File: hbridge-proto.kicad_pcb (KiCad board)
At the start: 2 copper layers, 126 x 72 mm, 45 parts, among them IC1 LM5106, IC2 LM5106, J1 Screw_Terminal_1x03, J2 Screw_Terminal_1x02, J3 Screw_Terminal_1x02, J4 Screw_Terminal_1x02, Q1 TO-220-DUAL, Q2 TO-220-DUAL, Q3 TO-220-DUAL, Q4 TO-220-DUAL

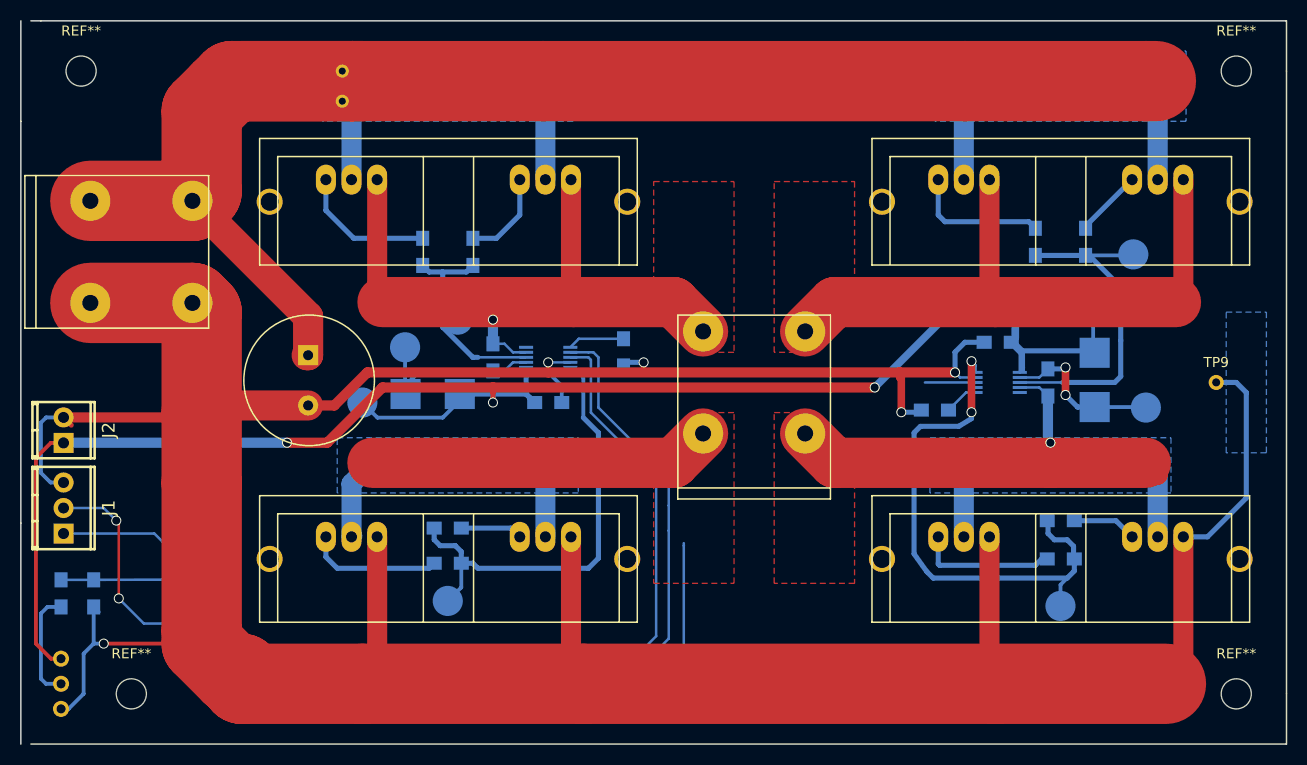
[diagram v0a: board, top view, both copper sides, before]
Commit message: Improved driver signal routing
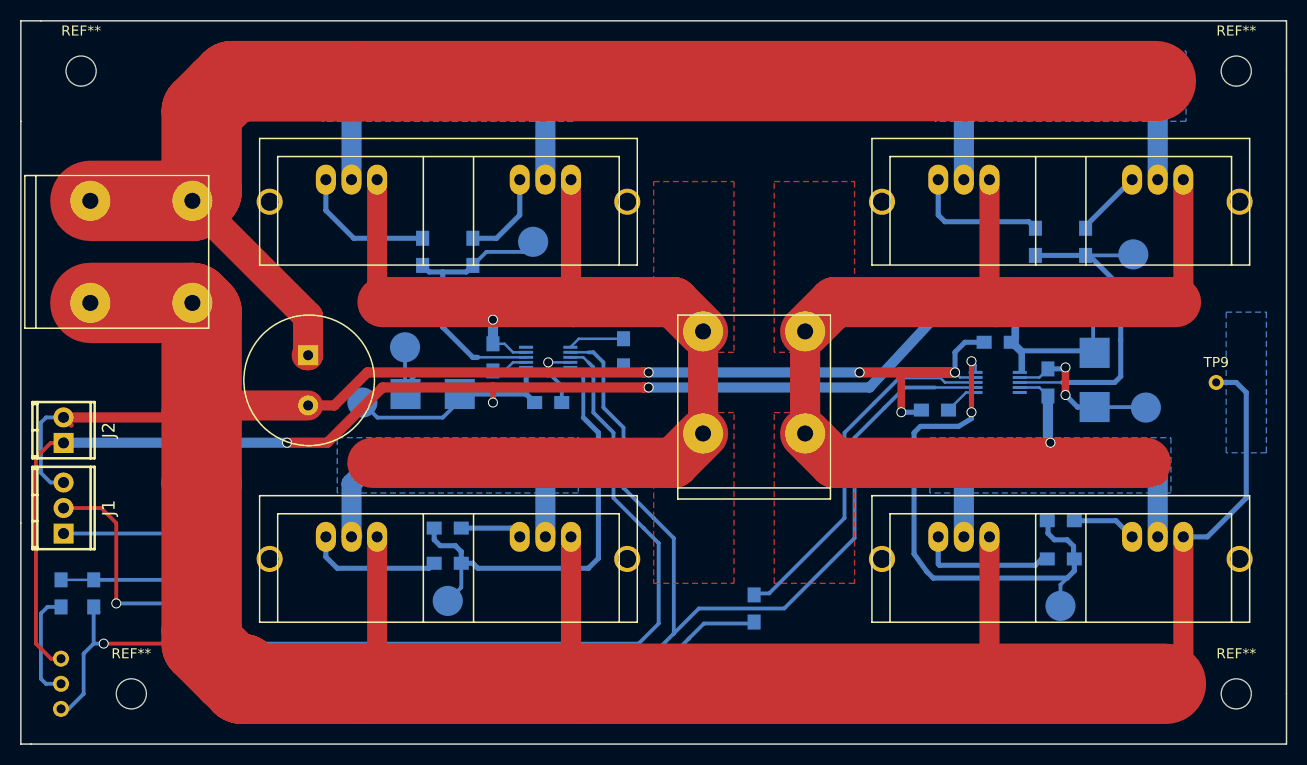
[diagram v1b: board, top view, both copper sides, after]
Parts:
- removed the REF** at (105.0, 67.0)
- removed the REF** at (105.0, 70.0)
- added R12: 0, Resistors_SMD:R_0805_HandSoldering, B.Cu at (146.0, 120.5)
- moved TP3 10.8 mm to (124.0, 84.0)
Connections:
- IC2 pad 8: /DRV_2_IN -> /DRV_2_IN_JMP
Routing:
- net /DRV_EN: track 102.9 -> 147.3 mm
- net +12V: track 257.0 -> 218.6 mm
- net /DRV_2_IN_JMP: track 0.00 -> 36.1 mm
- net GND: track 439.8 -> 420.4 mm, vias 5 -> 6
- net /MOTOR-: track 132.2 -> 142.4 mm
- net /MOTOR+: track 113.1 -> 123.3 mm
- net /DRV_2_IN: track 91.1 -> 84.1 mm, vias 2 -> 1
- net Net-(IC1-Pad3): track 28.5 -> 33.6 mm
- net /DRV_1_IN: track 101.2 -> 98.7 mm
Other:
- outline, holes or cut-outs redrawn

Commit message: final version before via stitching
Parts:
- moved J3 1.50 mm to (85.0, 86.5)
- moved C4 1.35 mm to (100.5, 97.0)
- moved D2 0.25 mm to (178.0, 97.8)
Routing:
- net GND: track 420.4 -> 489.0 mm, vias 6 -> 7
- net +24V: track 182.5 -> 242.3 mm
- net /MOTOR+: track 123.3 -> 180.8 mm
- net /MOTOR-: track 142.4 -> 195.8 mm
- net +12V: track 218.6 -> 223.0 mm
- net Net-(IC2-Pad10): track 57.7 -> 61.4 mm
- net /DRV_2_IN: track 84.1 -> 83.2 mm
- added copper zone on F.Cu, net +24V
- added copper zone on F.Cu, net GND
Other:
- net class Default: via_dia 1 -> 1.4

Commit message: version 1 submitted for fab
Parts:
- added REF**: VIA-1.1MM, Hbridge_proto:VIA-1.1MM, F.Cu at (120.5, 68.5)
- added REF**: VIA-1.1MM, Hbridge_proto:VIA-1.1MM, F.Cu at (105.5, 106.0)
- added REF**: VIA-1.1MM, Hbridge_proto:VIA-1.1MM, F.Cu at (108.5, 106.0)
- added REF**: VIA-1.1MM, Hbridge_proto:VIA-1.1MM, F.Cu at (111.5, 106.0)
- added REF**: VIA-1.1MM, Hbridge_proto:VIA-1.1MM, F.Cu at (127.0, 106.0)
- added REF**: VIA-1.1MM, Hbridge_proto:VIA-1.1MM, F.Cu at (124.0, 106.0)
- added REF**: VIA-1.1MM, Hbridge_proto:VIA-1.1MM, F.Cu at (121.0, 106.0)
- added REF**: VIA-1.1MM, Hbridge_proto:VIA-1.1MM, F.Cu at (165.0, 106.0)
- added REF**: VIA-1.1MM, Hbridge_proto:VIA-1.1MM, F.Cu at (168.0, 106.0)
- added REF**: VIA-1.1MM, Hbridge_proto:VIA-1.1MM, F.Cu at (171.0, 106.0)
- added REF**: VIA-1.1MM, Hbridge_proto:VIA-1.1MM, F.Cu at (187.0, 106.0)
- added REF**: VIA-1.1MM, Hbridge_proto:VIA-1.1MM, F.Cu at (184.0, 106.0)
- added REF**: VIA-1.1MM, Hbridge_proto:VIA-1.1MM, F.Cu at (181.0, 106.0)
- added REF**: VIA-1.1MM, Hbridge_proto:VIA-1.1MM, F.Cu at (187.5, 68.5)
- added REF**: VIA-1.1MM, Hbridge_proto:VIA-1.1MM, F.Cu at (184.5, 68.5)
- added REF**: VIA-1.1MM, Hbridge_proto:VIA-1.1MM, F.Cu at (181.5, 68.5)
- added REF**: VIA-1.1MM, Hbridge_proto:VIA-1.1MM, F.Cu at (165.5, 68.5)
- added REF**: VIA-1.1MM, Hbridge_proto:VIA-1.1MM, F.Cu at (168.5, 68.5)
- added REF**: VIA-1.1MM, Hbridge_proto:VIA-1.1MM, F.Cu at (171.5, 68.5)
- added REF**: VIA-1.1MM, Hbridge_proto:VIA-1.1MM, F.Cu at (113.5, 68.5)
- added REF**: VIA-1.1MM, Hbridge_proto:VIA-1.1MM, F.Cu at (117.5, 68.5)
- added REF**: VIA-1.1MM, Hbridge_proto:VIA-1.1MM, F.Cu at (114.5, 106.0)
- added REF**: VIA-1.1MM, Hbridge_proto:VIA-1.1MM, F.Cu at (118.0, 106.0)
- added REF**: VIA-1.1MM, Hbridge_proto:VIA-1.1MM, F.Cu at (174.5, 68.5)
- added REF**: VIA-1.1MM, Hbridge_proto:VIA-1.1MM, F.Cu at (178.5, 68.5)
- added REF**: VIA-1.1MM, Hbridge_proto:VIA-1.1MM, F.Cu at (174.0, 106.0)
- added REF**: VIA-1.1MM, Hbridge_proto:VIA-1.1MM, F.Cu at (178.0, 106.0)
- added REF**: VIA-1.1MM, Hbridge_proto:VIA-1.1MM, F.Cu at (104.5, 68.5)
- added REF**: VIA-1.1MM, Hbridge_proto:VIA-1.1MM, F.Cu at (107.5, 68.5)
- added REF**: VIA-1.1MM, Hbridge_proto:VIA-1.1MM, F.Cu at (126.5, 68.5)
- added REF**: VIA-1.1MM, Hbridge_proto:VIA-1.1MM, F.Cu at (123.5, 68.5)
- added REF**: VIA-1.1MM, Hbridge_proto:VIA-1.1MM, F.Cu at (110.5, 68.5)
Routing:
- net /MOTOR-: vias 3 -> 2
